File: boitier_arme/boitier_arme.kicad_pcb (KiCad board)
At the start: 2 copper layers, 50 x 49.6 mm, 7 parts, among them J1 Conn_01x02_Pin, U1 XIAO-nRF52840-SMD

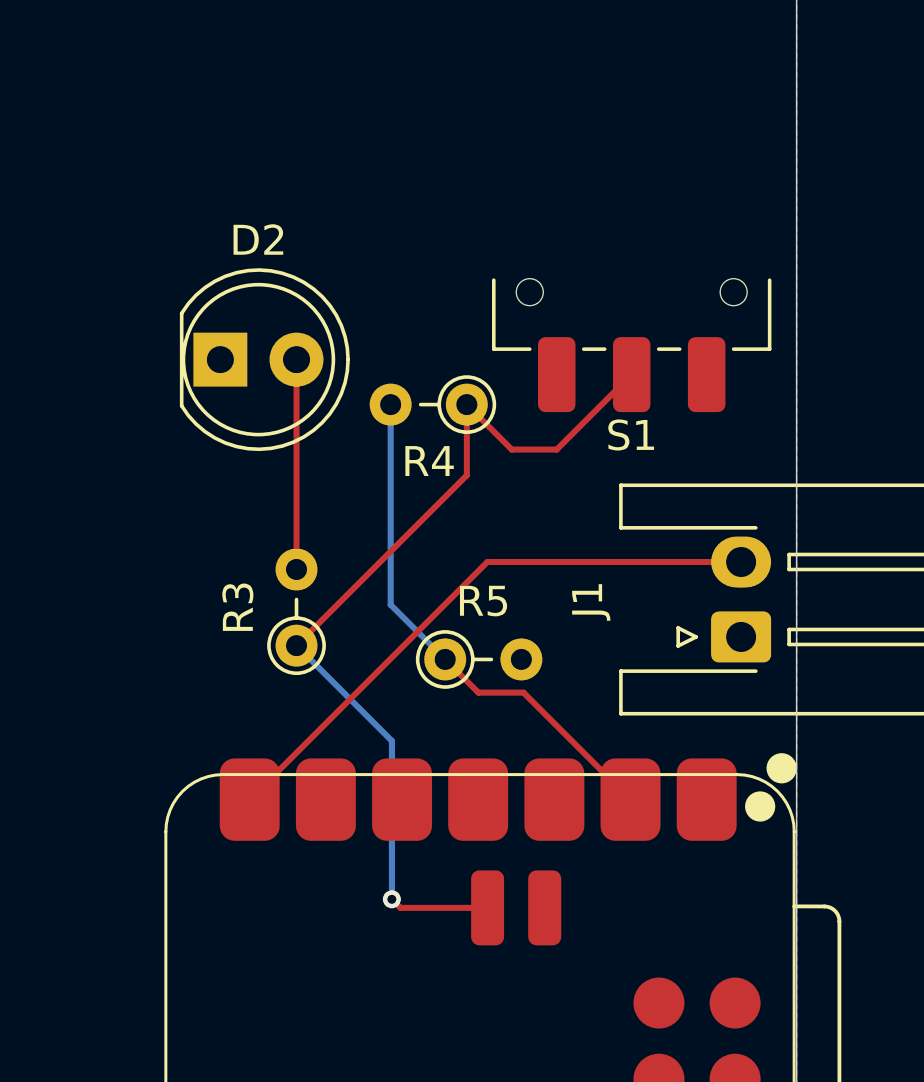
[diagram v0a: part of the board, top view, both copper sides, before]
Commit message: batterie rajouté
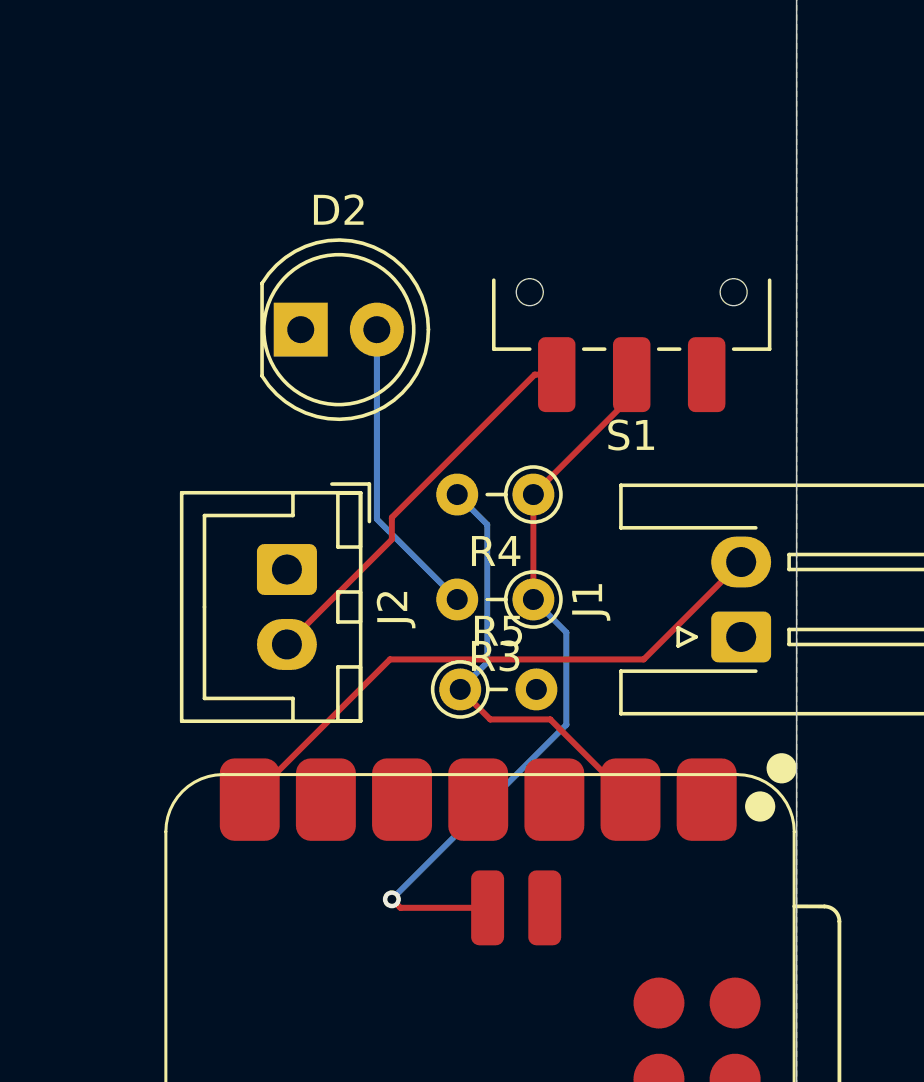
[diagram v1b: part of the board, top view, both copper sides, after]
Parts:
- added J2: Battery, Connector_JST:JST_XH_B2B-XH-A_1x02_P2.50mm_Vertical, F.Cu at (144.0, 82.5)
- moved R3 8.05 mm to (152.2, 83.5), turned to 180 degrees
- moved R4 3.73 mm to (152.2, 80.0)
- moved D2 2.86 mm to (144.5, 74.5)
- moved R5 1.12 mm to (149.8, 86.5)
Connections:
- S1 pad 3: unconnected-(S1-Pad3) -> Net-(J2-Pin_2)
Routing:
- net Net-(J2-Pin_2): track 0.00 -> 13.2 mm
- net /BAT+: track 30.6 -> 25.0 mm
- net Net-(D2-A): track 7.00 -> 10.1 mm
- net /BAT_level: track 17.4 -> 14.5 mm

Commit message: a jour
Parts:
- J1: footprint Connector_JST:JST_XH_S2B-XH-A-1_1x02_P2.50mm_Horizontal -> Connector_JST:JST_XH_B2B-XH-A_1x02_P2.50mm_Vertical
- J2: value Battery -> 125SH-B-02-TS; footprint Connector_JST:JST_XH_B2B-XH-A_1x02_P2.50mm_Vertical -> footprints:CONN_125SH-B-02-TS_ADM
- moved S1 4.85 mm to (150.7, 73.3)
- moved D2 3.95 mm to (140.7, 75.8)
- moved J2 2.21 mm to (142.5, 84.1)
- moved U1 0.38 mm to (150.4, 97.9)
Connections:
- J2 pad 1: GND -> Net-(J2-Pad1)
- J2 pad 2: Net-(J2-Pin_2) -> GND
- S1 pad 3: Net-(J2-Pin_2) -> Net-(J2-Pad1)
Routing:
- net Net-(J2-Pin_2): track 13.2 -> 0.00 mm
- net Net-(J2-Pad1): track 0.00 -> 10.5 mm
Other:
- board size 50 x 49.6 mm -> 26.9 x 35.7 mm

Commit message: a jour
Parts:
- J1: footprint Connector_JST:JST_XH_B2B-XH-A_1x02_P2.50mm_Vertical -> Connector_JST:JST_XH_S2B-XH-A-1_1x02_P2.50mm_Horizontal

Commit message: Changement suite au retour du GUS
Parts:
- added H1: MountingHole, MountingHole:MountingHole_3.5mm, F.Cu at (136.4, 74.8)
- added H2: MountingHole, MountingHole:MountingHole_3.5mm, F.Cu at (158.1, 74.8)
- added H3: MountingHole, MountingHole:MountingHole_3.5mm, F.Cu at (136.5, 104.9)
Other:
- outline, holes or cut-outs redrawn
